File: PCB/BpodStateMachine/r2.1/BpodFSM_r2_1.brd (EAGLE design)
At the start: 99.9 x 76.2 mm, 46 parts, among them IC1 SN65HVD31DR, IC10 MTU1D0505MC, IC11 MTU1D0505MC, IC2 SN65HVD31DR, IC3 SN65HVD31DR, IC4 SN65HVD31DR, IC5 SN65HVD31DR, IC6 OPTOISOLATOR-2SOIC8, IC7 ADUM5240, IC9 MTU1D0505MC

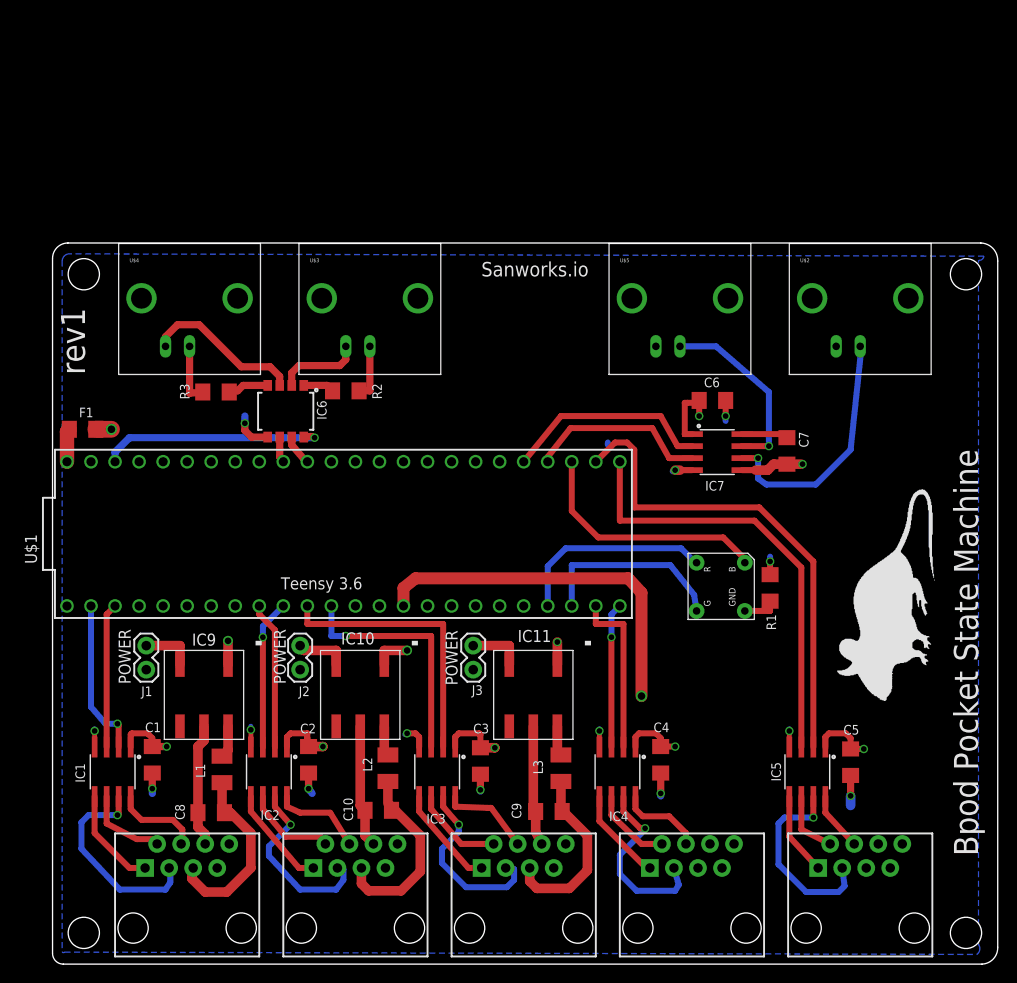
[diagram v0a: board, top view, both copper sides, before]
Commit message: -Updated PCB designs for all boards with Teensy 3.5 + 3.6 to optimize solder pads for assembly (new designs validated 12 JAN 2018). No components changed. -Optimized silk screens on PCBs above to ensure that each component name is clearly visible (previously overlapped with vias in some cases) -Improved design of Bpod 2 enclosure for added mechanical strength
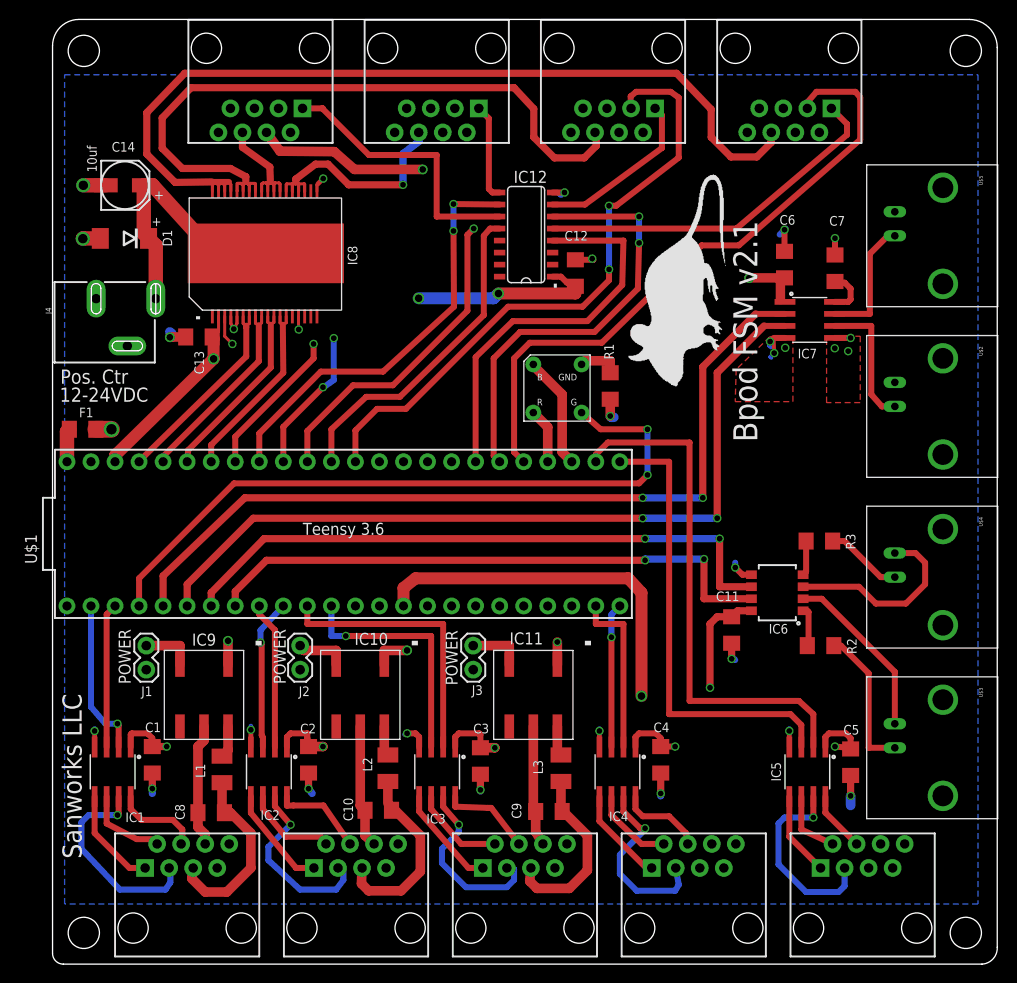
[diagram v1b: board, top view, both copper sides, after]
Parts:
- added C11, C12, C13: 0.1uf, SparkFun-Capacitors:1206
- added C14: EEE-FK1H100UR, JoshParts10:EEE-FK1H100UR
- added D1: (no value), diode:DO214AA
- added IC12: CD4050, SparkFun-DigitalIC:SO16
- added IC8: ISO1H811G, JoshParts10:ISO1H811G
- added J4: POWER_JACKSLT, SparkFun-Connectors:POWER_JACK_SLOT
- added PORT1, PORT2, PORT3, PORT4: RJ45-8PTH, SparkFun:RJ45-8
- R2, R3: value 220 -> 1K
- moved U$4 78.4 mm to (89.0, 40.9), turned to 270 degrees
- moved U$3 69.8 mm to (89.0, 22.9), turned to 270 degrees
- moved R3 65.7 mm to (81.0, 44.7), turned to 0 degrees
- moved R2 56.9 mm to (81.2, 33.7)
- moved IC6 55.4 mm to (76.6, 39.2), turned to 90 degrees
- moved U$9 39.9 mm to (59.0, 59.1)
- moved U$8 30.6 mm to (50.8, 63.4), turned to 180 degrees
- moved R1 27.2 mm to (58.9, 61.1), turned to 90 degrees
- moved U$5 25.5 mm to (89.0, 77.0), turned to 270 degrees
- moved JP4 23.6 mm to (96.5, 96.5)
- moved JP3 23.6 mm to (3.30, 96.5)
- moved C7 20.0 mm to (82.7, 73.5), turned to 270 degrees
- moved IC7 17.1 mm to (80.0, 68.1)
- moved C6 16.2 mm to (77.3, 73.9), turned to 270 degrees
- moved U$2 7.33 mm to (89.0, 58.9), turned to 270 degrees
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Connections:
- new net BNCOUT1: IC7.3, U$1.4
- new net BNCOUT2: IC7.2, U$1.3
- new net DRVR_ENBL: IC8.P$3, U$1.19/A5
- new net GNDBB: C14.CATHODE, D1.A, IC8.P$19, J4.GND@1, J4.GND@2, PORT1.7, PORT2.7, PORT3.7, PORT4.7
- new net N$31: IC12.11, PORT4.1
- new net N$56: IC12.5, PORT1.1
- new net PORT1IN: IC12.4, U$1.39/A20
- new net PORT1LED: PORT1.3, U$1.37/A18
- new net PORT2IN: IC12.6, U$1.38/A19
- new net PORT2LED: PORT2.3, U$1.14/A0
- new net PORT3IN: IC12.10, U$1.18/A4
- new net PORT3LED: PORT3.3, U$1.16/A2
- new net PORT4IN: IC12.12, U$1.15/A1
- new net PORT4LED: PORT4.3, U$1.17/A3
- new net VBB: C14.ANODE, D1.C, IC8.VBB, J4.PWR
- new net VLV1IN: IC8.P$6, IC8.P$7, U$1.23/A9
- new net VLV1OUT: IC8.P$33, IC8.P$34, IC8.P$35, IC8.P$36, PORT1.6
- new net VLV2IN: IC8.P$8, IC8.P$9, U$1.22/A8
- new net VLV2OUT: IC8.P$29, IC8.P$30, IC8.P$31, IC8.P$32, PORT2.6
- new net VLV3IN: IC8.P$12, IC8.P$13, U$1.20/A6
- new net VLV3OUT: IC8.P$21, IC8.P$22, IC8.P$23, IC8.P$24, PORT3.6
- new net VLV4IN: IC8.P$10, IC8.P$11, U$1.21/A7
- new net VLV4OUT: IC8.P$25, IC8.P$26, IC8.P$27, IC8.P$28, PORT4.6
- net 5V: now also PORT1.4, PORT2.4, PORT3.4, PORT4.4
- net BNCIN1: now also U$1.6; no longer U$1.16/A2
- net BNCIN2: now also U$1.5; no longer U$1.17/A3
- net GND: now also C11.2, C12.1, C13.2, IC12.8, IC8.P$15, IC8.P$4, IC8.P$5, PORT1.5, PORT2.5, PORT3.5, PORT4.5
- net LED_GREEN: now also U$1.2; no longer U$1.30
- net LED_RED: now also U$1.36/A17; no longer U$1.29
- net N$20: now also IC12.7, PORT2.1; no longer IC7.3, U$1.36/A17
- net N$24: now also IC12.9, PORT3.1; no longer IC7.2, U$1.37/A18
- net VCC: now also C11.1, C12.2, C13.1, IC12.1, IC8.P$2
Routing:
- net 5V: track 21.1 -> 149.8 mm, vias 5 -> 6
- net VLV1OUT: track 0.00 -> 94.8 mm
- net BNCOUT2: track 0.00 -> 88.4 mm, vias 0 -> 2
- net BNCOUT1: track 0.00 -> 85.8 mm, vias 0 -> 2
- net VLV2OUT: track 0.00 -> 74.3 mm
- net PORT1LED: track 0.00 -> 68.4 mm
- net PORT2LED: track 0.00 -> 66.7 mm, vias 0 -> 2
- net BNCIN2: track 2.73 -> 66.0 mm, vias 0 -> 2
- net BNCIN1: track 3.29 -> 61.8 mm, vias 0 -> 2
- net PORT3LED: track 0.00 -> 58.2 mm, vias 0 -> 1
- net VCC: track 100.2 -> 154.7 mm, vias 7 -> 10
- net LED_GREEN: track 20.5 -> 73.6 mm, vias 0 -> 2
- net PORT4LED: track 0.00 -> 51.8 mm, vias 0 -> 2
- net PORT2IN: track 0.00 -> 46.2 mm, vias 0 -> 2
- net PORT3IN: track 0.00 -> 44.7 mm, vias 0 -> 2
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- added copper zone on layer 1, net GND
- added copper zone on layer 15, net GNDBB
- added copper zone on layer 1, net ISOGND
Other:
- board size 99.9 x 76.2 mm -> 99.8 x 99.8 mm
- board text added: "+"
- board text added: "."
- board text added: "10uf"
- board text added: "12-24VDC"
- board text added: "Bpod FSM v2.1"
- board text added: "IC8"
- board text added: "Pos. Ctr"
- board text added: "Sanworks LLC"
- board text removed: "Bpod Pocket State Machine"
- board text removed: "Sanworks.io"
- board text removed: "rev1"
